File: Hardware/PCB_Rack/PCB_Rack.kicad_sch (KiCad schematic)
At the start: 39 parts, among them J1 Conn_01x03, SW1 SW_SPST, SW2 SW_SPST, U3 PCF8575DBR

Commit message: Correction footprint connecteurs
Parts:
- H1, H2, H5, H6: footprint MountingHole:MountingHole_3.2mm_M3_DIN965_Pad_TopBottom -> MountingHole:MountingHole_2.2mm_M2_DIN965_Pad_TopBottom
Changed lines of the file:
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@@
 			)
 		)
-		(property "Footprint" "MountingHole:MountingHole_3.2mm_M3_DIN965_Pad_TopBottom"
+		(property "Footprint" "MountingHole:MountingHole_2.2mm_M2_DIN965_Pad_TopBottom"
 			(at 133.35 114.3 0)
 			(effects
@@
 			)
 		)
-		(property "Footprint" "MountingHole:MountingHole_3.2mm_M3_DIN965_Pad_TopBottom"
+		(property "Footprint" "MountingHole:MountingHole_2.2mm_M2_DIN965_Pad_TopBottom"
 			(at 114.3 157.48 0)
 			(effects
@@
 			)
 		)
-		(property "Footprint" "MountingHole:MountingHole_3.2mm_M3_DIN965_Pad_TopBottom"
+		(property "Footprint" "MountingHole:MountingHole_2.2mm_M2_DIN965_Pad_TopBottom"
 			(at 135.89 158.75 0)
 			(effects
@@
 			)
 		)
-		(property "Footprint" "MountingHole:MountingHole_3.2mm_M3_DIN965_Pad_TopBottom"
+		(property "Footprint" "MountingHole:MountingHole_2.2mm_M2_DIN965_Pad_TopBottom"
 			(at 115.57 114.3 0)
 			(effects

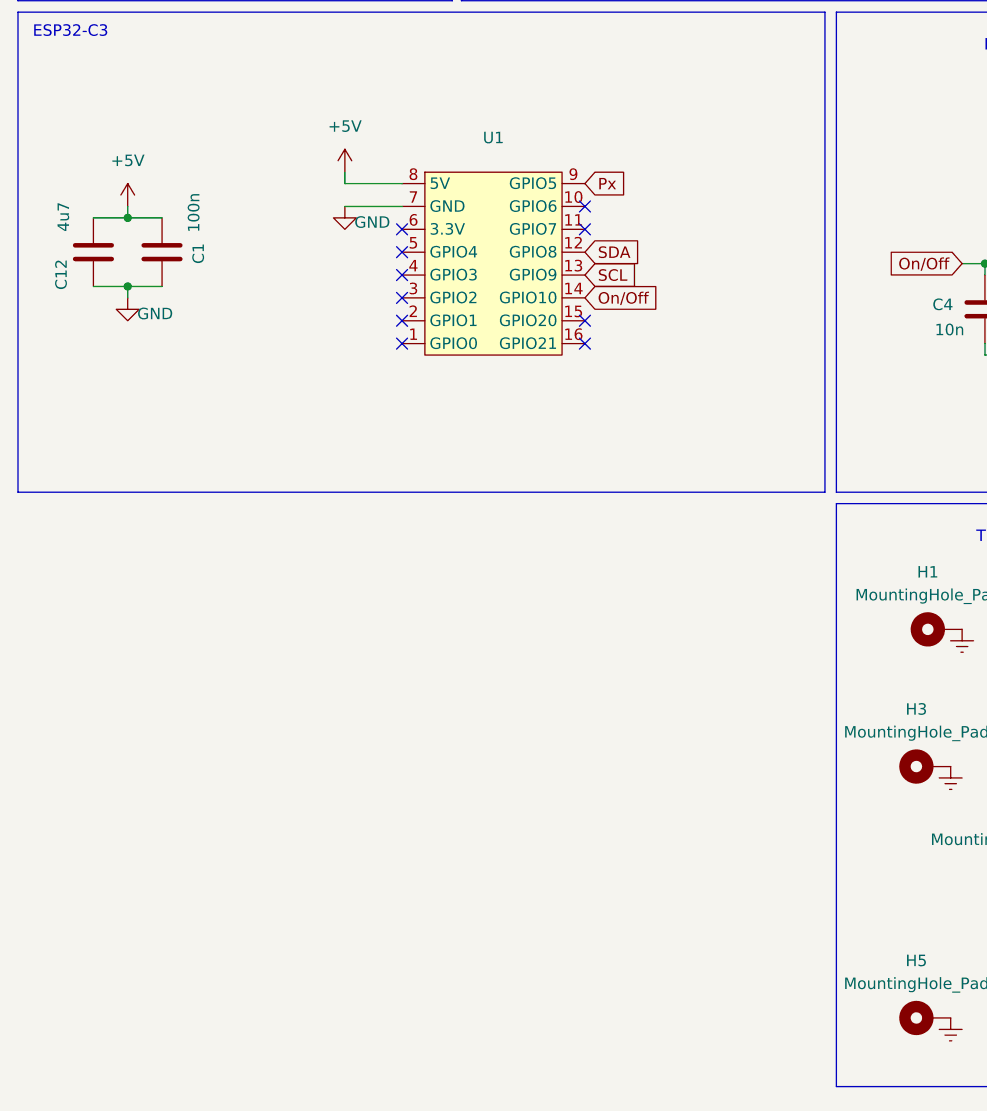
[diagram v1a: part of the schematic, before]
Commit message: ajout des pinheaders en plus
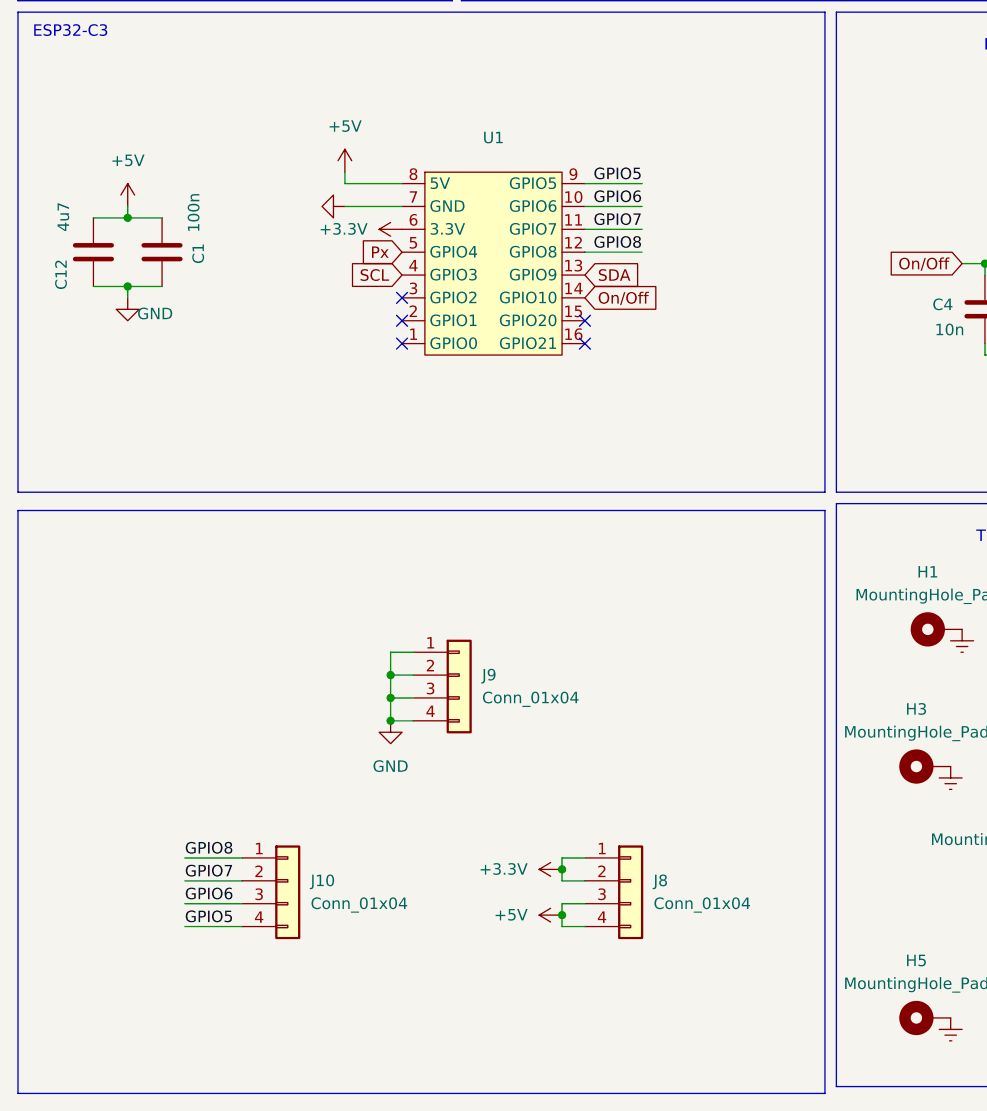
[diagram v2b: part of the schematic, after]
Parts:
- added J10, J8, J9: Conn_01x04, Connector_PinHeader_2.54mm:PinHeader_1x04_P2.54mm_Vertical, symbol Connector_Generic:Conn_01x04
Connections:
- net +5V: now also J8.3 (Pin_3), J8.4 (Pin_4)
- net GND: now also J9.1 (Pin_1), J9.2 (Pin_2), J9.3 (Pin_3), J9.4 (Pin_4)
- net Px: now also U1.5 (GPIO4); no longer U1.9 (GPIO5)
- net SCL: now also U1.4 (GPIO3); no longer U1.13 (GPIO9)
- net SDA: now also U1.13 (GPIO9); no longer U1.12 (GPIO8)
- net GPIO6: now reaches U1.10 (GPIO6)
- net GPIO6: now also J10.3 (Pin_3)
- net GPIO7: now reaches U1.11 (GPIO7)
- net GPIO7: now also J10.2 (Pin_2)
- net +3.3V: now reaches U1.6 (3.3V)
- net +3.3V: now also J8.1 (Pin_1), J8.2 (Pin_2)
- new net GPIO5: J10.4 (Pin_4), U1.9 (GPIO5)
- new net GPIO8: J10.1 (Pin_1), U1.12 (GPIO8)
- no-connect marks 16 -> 11

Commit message: correction orientation des connecteurs sur secteur
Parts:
- D2: footprint LED_SMD:LED_0603_1608Metric_Pad1.05x0.95mm_HandSolder -> img:LED_0603_avec_dessin
- D3: MPN (none) -> WS2812B
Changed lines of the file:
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@@
+			)
+		)
+		(property "MPN" "WS2812B"
+			(at 170.18 125.73 0)
+			(effects
+				(font
+					(size 1.27 1.27)
+				)
+				(hide yes)
 			)
 		)
@@
 			)
 		)
-		(property "Footprint" "LED_SMD:LED_0603_1608Metric_Pad1.05x0.95mm_HandSolder"
+		(property "Footprint" "img:LED_0603_avec_dessin"
 			(at 135.89 31.75 0)
 			(effects
@@
 			)
 		)
-		(property "Datasheet" "~"
+		(property "Datasheet" "https://www.we-online.com/components/products/datasheet/865060445005.pdf"
 			(at 106.68 33.02 0)
 			(effects

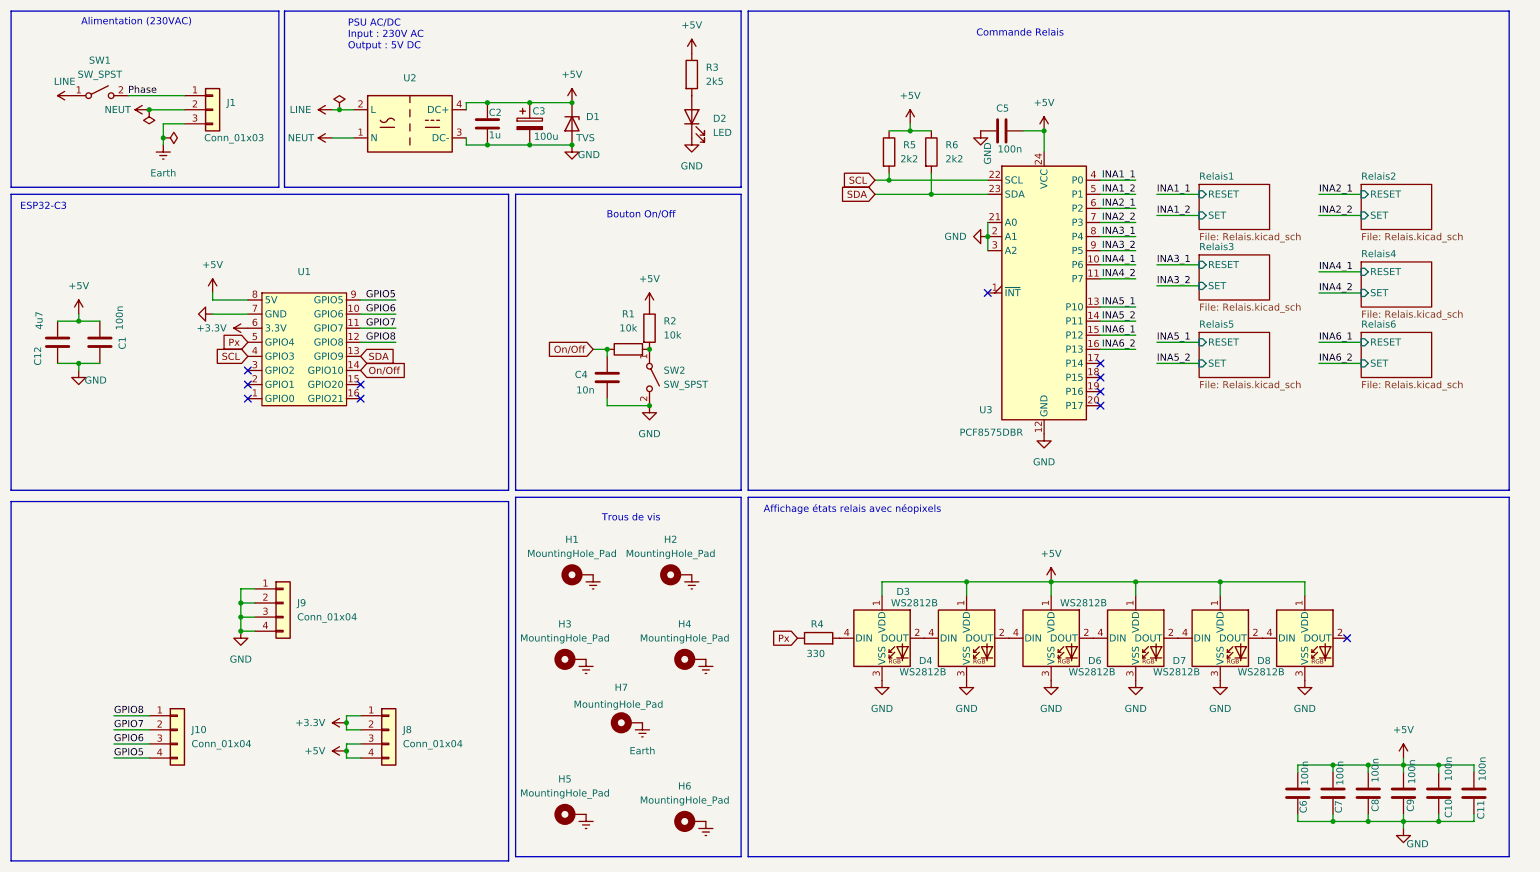
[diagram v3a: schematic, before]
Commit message: correction des pull-up sur SDA/SCL, finalisation du code esp32 Google_Calendar pour que la reconnexion (sur google device)se fasse automatiquement après reboot
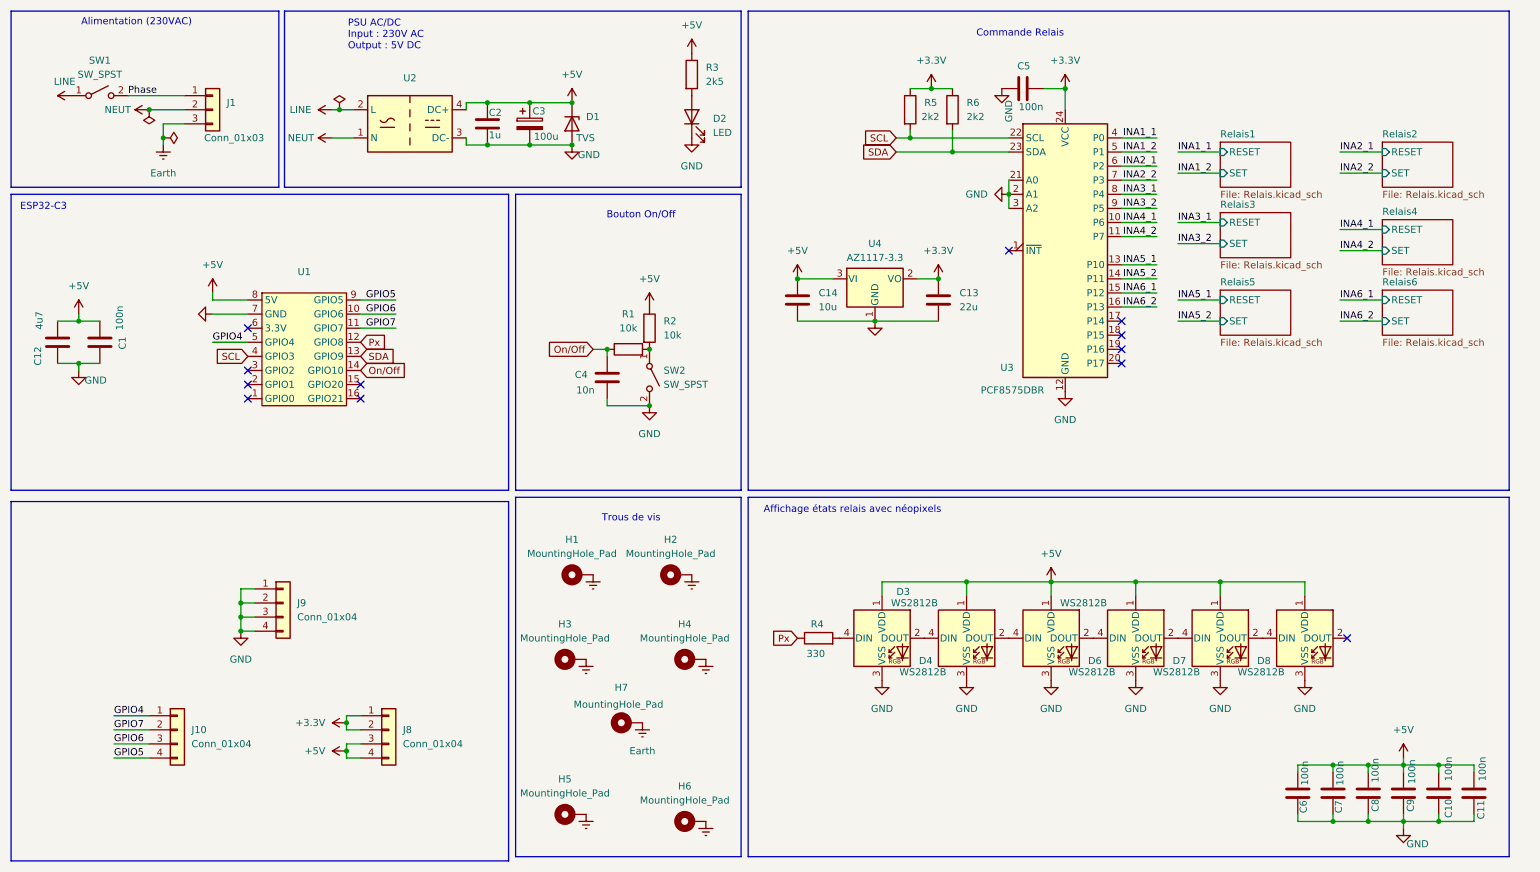
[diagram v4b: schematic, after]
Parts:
- added C13: 22u, Capacitor_SMD:C_0201_0603Metric_Pad0.64x0.40mm_HandSolder, symbol Device:C
- added C14: 10u, Capacitor_SMD:C_0201_0603Metric_Pad0.64x0.40mm_HandSolder, symbol Device:C
- added U4: AZ1117-3.3, Package_TO_SOT_SMD:SOT-223-3_TabPin2, symbol Regulator_Linear:AZ1117-3.3
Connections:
- net +3.3V: now also C5.2, R5.1, R6.1, U3.24 (VCC), C13.1, U4.2 (VO); no longer U1.6 (3.3V)
- net +5V: now also C14.1, U4.3 (VI); no longer C5.2, R5.1, R6.1, U3.24 (VCC)
- net GND: now also C13.2, C14.2, U4.1 (GND)
- net Px: now also U1.12 (GPIO8); no longer U1.5 (GPIO4)
- net GPIO8 renamed GPIO4
- net GPIO4: now also U1.5 (GPIO4); no longer U1.12 (GPIO8)
- no-connect marks 11 -> 12
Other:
- moved on the sheet: C5, R5, R6, U3
